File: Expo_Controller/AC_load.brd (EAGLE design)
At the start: 60 x 46 mm, 10 parts

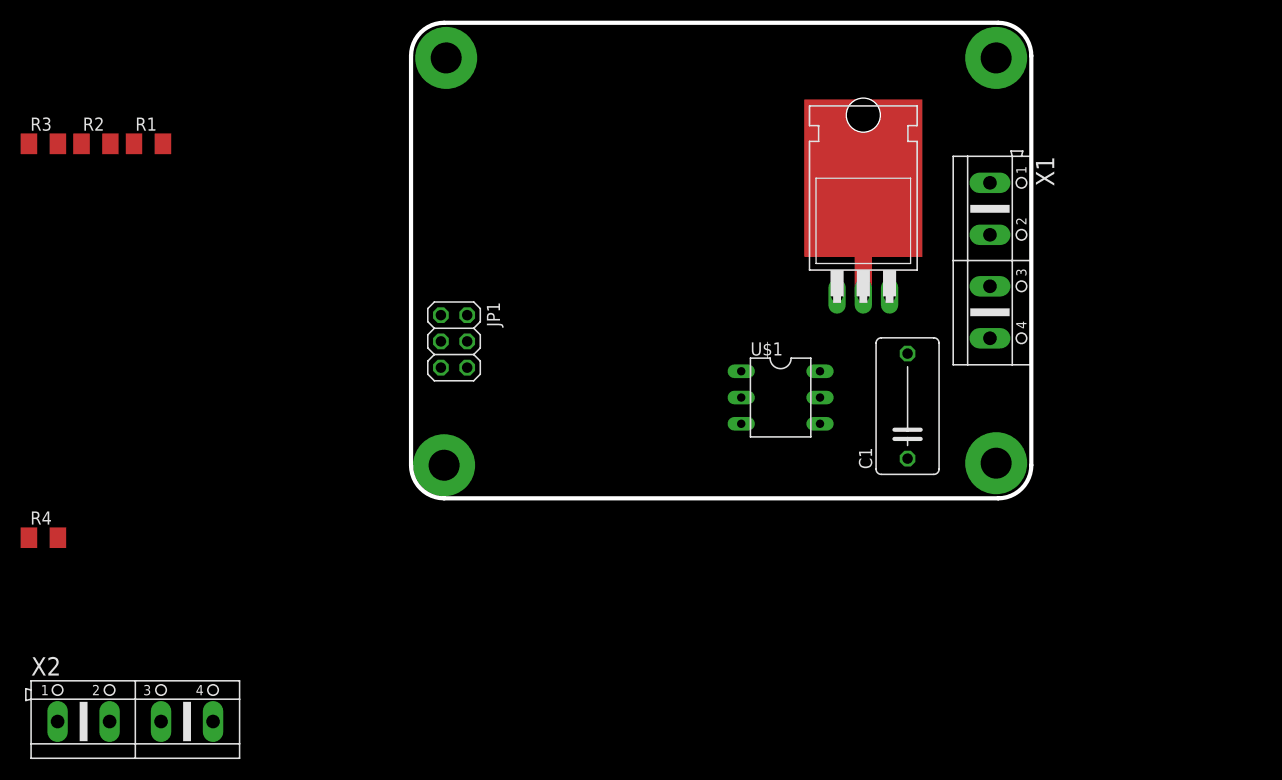
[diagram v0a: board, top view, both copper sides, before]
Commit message: Закончил разводку высоковольтного модуля
Signed-off-by: remixvit <remixvi@gmail.comt>
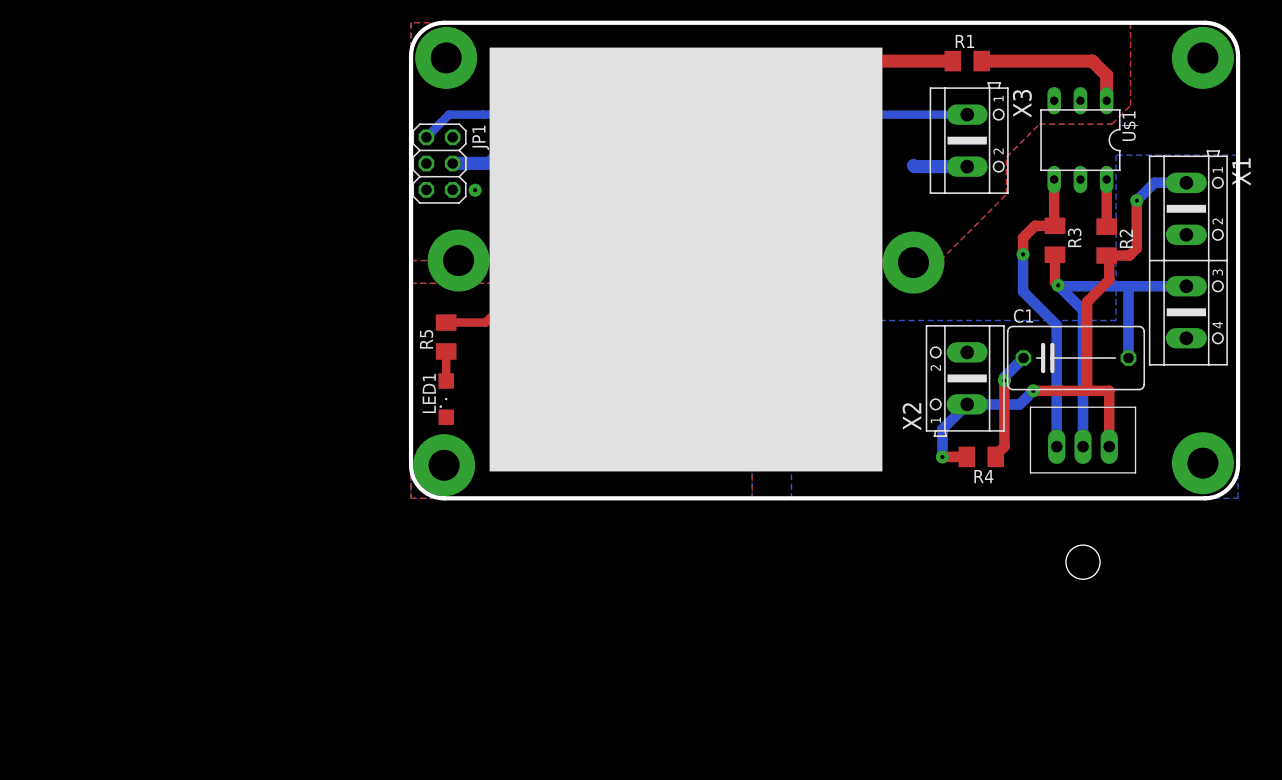
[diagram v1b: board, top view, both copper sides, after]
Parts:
- removed TRIAC1: BTB16_FLAT, Semistors:TO220AB
- added LED1: (no value), led:SML1206
- added R5: (no value), rcl:M1206
- added U$2: BTB16, Semistors:TO220
- added X3: (no value), con-ptr500:AK500/2
- X2: device con-ptr500:AK500/4 -> con-ptr500:AK500/2
- moved R3 98.3 mm to (62.3, 25.0), turned to 270 degrees
- moved R2 98.2 mm to (67.3, 24.9), turned to 270 degrees
- moved R4 91.1 mm to (55.2, 4.01), turned to 180 degrees
- moved X2 87.0 mm to (53.8, 11.6), turned to 90 degrees
- moved R1 79.6 mm to (53.8, 42.3)
- moved U$1 38.2 mm to (64.8, 34.6), turned to 180 degrees
- moved X1 19.0 mm to (75.0, 23.0)
- moved JP1 17.3 mm to (2.76, 32.4)
- moved C1 16.9 mm to (64.3, 13.6), turned to 0 degrees
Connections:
- new net N$14: LED1.A, R5.1
- net +12V: now also R5.2, X3.1; no longer X2.3
- net GND: now also JP1.2, LED1.C, X3.2; no longer X2.4
- net N$2: now also U$2.IN2; no longer TRIAC1.A2, TRIAC1.A2-PAD
- net N$4: now also U$2.CONTROL; no longer TRIAC1.G
- net V+: now also U$2.IN1; no longer TRIAC1.A1
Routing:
- net +12V: track 0.00 -> 78.2 mm, vias 0 -> 1
- net V+: track 0.00 -> 55.5 mm, vias 0 -> 3
- net N$3: track 0.00 -> 52.5 mm, vias 0 -> 1
- net N$4: track 0.00 -> 29.6 mm, vias 0 -> 1
- net N$2: track 11.4 -> 39.1 mm, vias 0 -> 1
- net N$1: track 0.00 -> 15.1 mm
- net GND: track 0.00 -> 10.8 mm, vias 0 -> 1
- net N$7: track 0.00 -> 10.7 mm, vias 0 -> 1
- net N$6: track 0.00 -> 4.56 mm
- net N$14: track 0.00 -> 2.85 mm
- added copper zone on layer 1, net GND
- added copper zone on layer 16, net GND
- added copper zone on layer 16, net PE
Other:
- board size 60 x 46 mm -> 80 x 46 mm

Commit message: BugFix
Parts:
- U$2: device Semistors:TO220 -> Semistors:TO220NORM
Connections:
- net N$2: now also U$2.MT1; no longer U$2.IN2
- net N$4: now also U$2.GATE; no longer U$2.CONTROL
- net V+: now also U$2.MT2; no longer U$2.IN1
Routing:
- net N$2: track 39.1 -> 31.8 mm
- net V+: track 55.5 -> 53.5 mm, vias 3 -> 4
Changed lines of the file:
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@@
 <?xml version="1.0" encoding="utf-8"?>
 <!DOCTYPE eagle SYSTEM "eagle.dtd">
-<eagle version="7.1.0">
+<eagle version="6.5.0">
 <drawing>
 <settings>
@@
 <pass name="Default">
 <param name="RoutingGrid" value="50mil"/>
-<param name="AutoGrid" value="1"/>
-<param name="Efforts" value="0"/>
-<param name="TopRouterVariant" value="1"/>
 <param name="tpViaShape" value="round"/>
 <param name="PrefDir.1" value="|"/>
@@
 <attribute name="OC_FARNELL" value="unknown" x="53.8" y="34.6" size="1.778" layer="27" rot="R270" display="off"/>
 </element>
-<element name="U$2" library="Semistors" package="TO220" value="BTB16" x="65" y="5" rot="R180"/>
+<element name="U$2" library="Semistors" package="TO220NORM" value="BTB16" x="65" y="5" rot="R180"/>
 <element name="LED1" library="led" package="SML1206" value="" x="3.4" y="9.6" rot="R90"/>
 <element name="R5" library="rcl" package="M1206" value="" x="3.4" y="15.6" rot="R90"/>
@@
 <contactref element="R4" pad="2"/>
 <contactref element="X2" pad="1"/>
-<contactref element="U$2" pad="IN1"/>
+<contactref element="U$2" pad="MT2"/>
 <wire x1="75" y1="30.5184" x2="71.9184" y2="30.5184" width="1.016" layer="16"/>
 <wire x1="71.9184" y1="30.5184" x2="70.2" y2="28.8" width="1.016" layer="16"/>
@@
 <wire x1="70.2" y1="24.2" x2="69.48" y2="23.48" width="1.016" layer="1"/>
 <wire x1="69.48" y1="23.48" x2="67.29" y2="23.48" width="1.016" layer="1"/>
-<wire x1="67.54" y1="5" x2="67.54" y2="10.4" width="1.016" layer="1"/>
 <wire x1="67.54" y1="23.23" x2="67.29" y2="23.48" width="1.016" layer="1"/>
 <wire x1="53.8" y1="9.0854" x2="58.8854" y2="9.0854" width="1.016" layer="16"/>
@@
 <via x="60.2" y="10.4" extent="1-16" drill="0.4" diameter="1.27"/>
 <wire x1="60.2" y1="10.4" x2="65.4" y2="10.4" width="1.016" layer="1"/>
-<wire x1="65.4" y1="10.4" x2="67.54" y2="10.4" width="1.016" layer="1"/>
 <wire x1="53.76" y1="4.01" x2="51.41" y2="4.01" width="1.016" layer="1"/>
 <wire x1="51.41" y1="4.01" x2="51.4" y2="4" width="1.016" layer="1"/>
@@
 <wire x1="67.54" y1="23.23" x2="67.54" y2="21.14" width="1.016" layer="1"/>
 <wire x1="67.54" y1="21.14" x2="65.4" y2="19" width="1.016" layer="1"/>
-<wire x1="65.4" y1="19" x2="65.4" y2="10.4" width="1.016" layer="1"/>
+<wire x1="65.4" y1="19" x2="65.4" y2="11.6" width="1.016" layer="1"/>
+<wire x1="65" y1="5" x2="65" y2="10" width="1.016" layer="16"/>
+<wire x1="65" y1="10" x2="65.4" y2="10.4" width="1.016" layer="16"/>
+<via x="65.4" y="10.4" extent="1-16" drill="0.4" diameter="1.27"/>
+<wire x1="65.4" y1="10.4" x2="65.4" y2="11.6" width="1.016" layer="1"/>
 </signal>
 <signal name="PE">
@@
 <contactref element="C1" pad="2"/>
 <contactref element="X1" pad="3"/>
-<contactref element="U$2" pad="IN2"/>
+<contactref element="U$2" pad="MT1"/>
 <wire x1="75" y1="20.5108" x2="69.4" y2="20.5108" width="1.016" layer="16"/>
 <wire x1="69.4" y1="20.5108" x2="62.6892" y2="20.5108" width="1.016" layer="16"/>
@@
 <wire x1="62.6" y1="20.6" x2="62.29" y2="20.91" width="1.016" layer="1"/>
 <wire x1="62.29" y1="20.91" x2="62.29" y2="23.56" width="1.016" layer="1"/>
-<wire x1="65" y1="5" x2="65" y2="18.2" width="1.016" layer="16"/>
-<wire x1="65" y1="18.2" x2="62.6" y2="20.6" width="1.016" layer="16"/>
 <wire x1="69.4" y1="13.57" x2="69.4" y2="20.5108" width="1.016" layer="16"/>
+<wire x1="67.54" y1="5" x2="67.54" y2="9.34" width="1.016" layer="16"/>
+<wire x1="67.54" y1="9.34" x2="69.4" y2="11.2" width="1.016" layer="16"/>
+<wire x1="69.4" y1="11.2" x2="69.4" y2="13.57" width="1.016" layer="16"/>
 </signal>
 <signal name="N$4">
 <contactref element="U$1" pad="4"/>
 <contactref element="R3" pad="1"/>
-<contactref element="U$2" pad="CONTROL"/>
+<contactref element="U$2" pad="GATE"/>
 <wire x1="62.21" y1="30.84" x2="62.21" y2="26.44" width="1.016" layer="1"/>
 <wire x1="62.21" y1="26.44" x2="62.29" y2="26.36" width="1.016" layer="1"/>
